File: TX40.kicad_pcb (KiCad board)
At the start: 2 copper layers, 85 x 50 mm, 16 parts, among them J1 691111710002, J2 691111710002, J3 691111710002, J4 691111710002, J5 691111710002, J6 691111710002, K1 SRD-05VDC-SL-C, K2 SRD-05VDC-SL-C

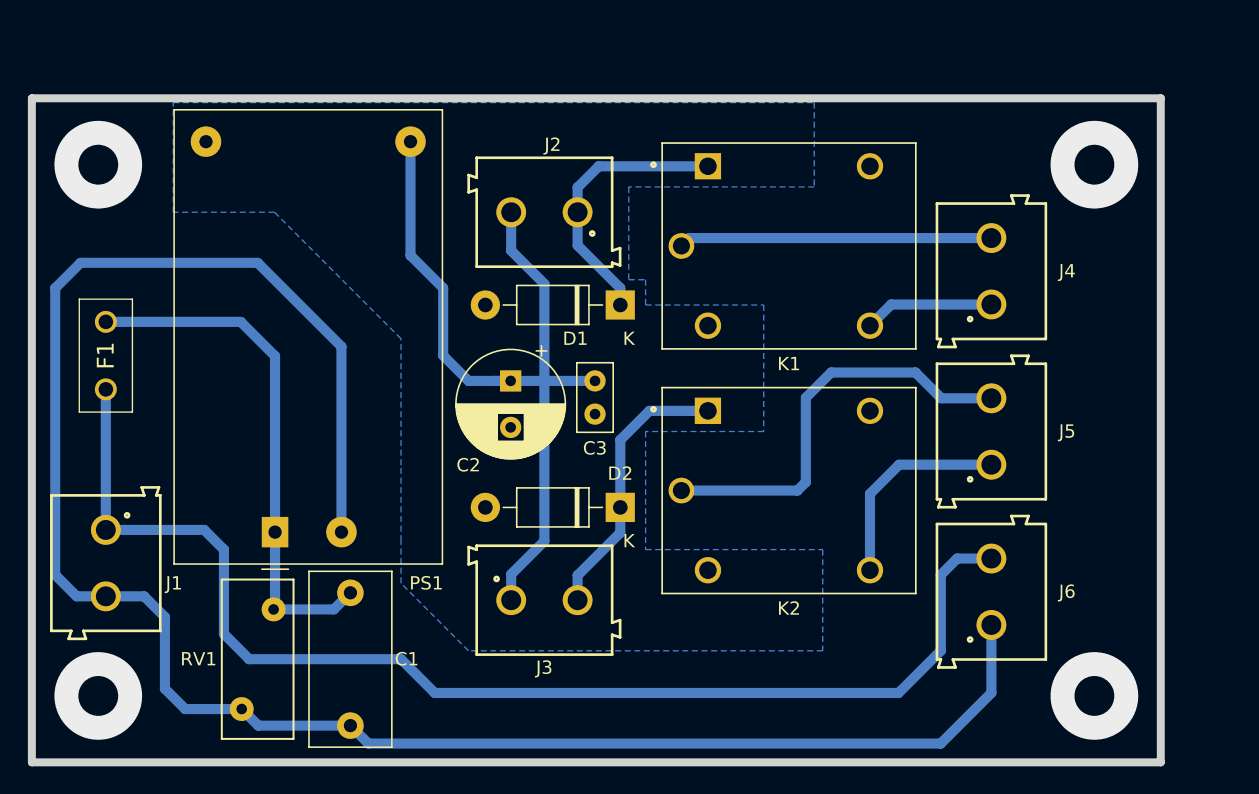
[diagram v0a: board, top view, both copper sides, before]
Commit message: Cambio a placa de 55x90
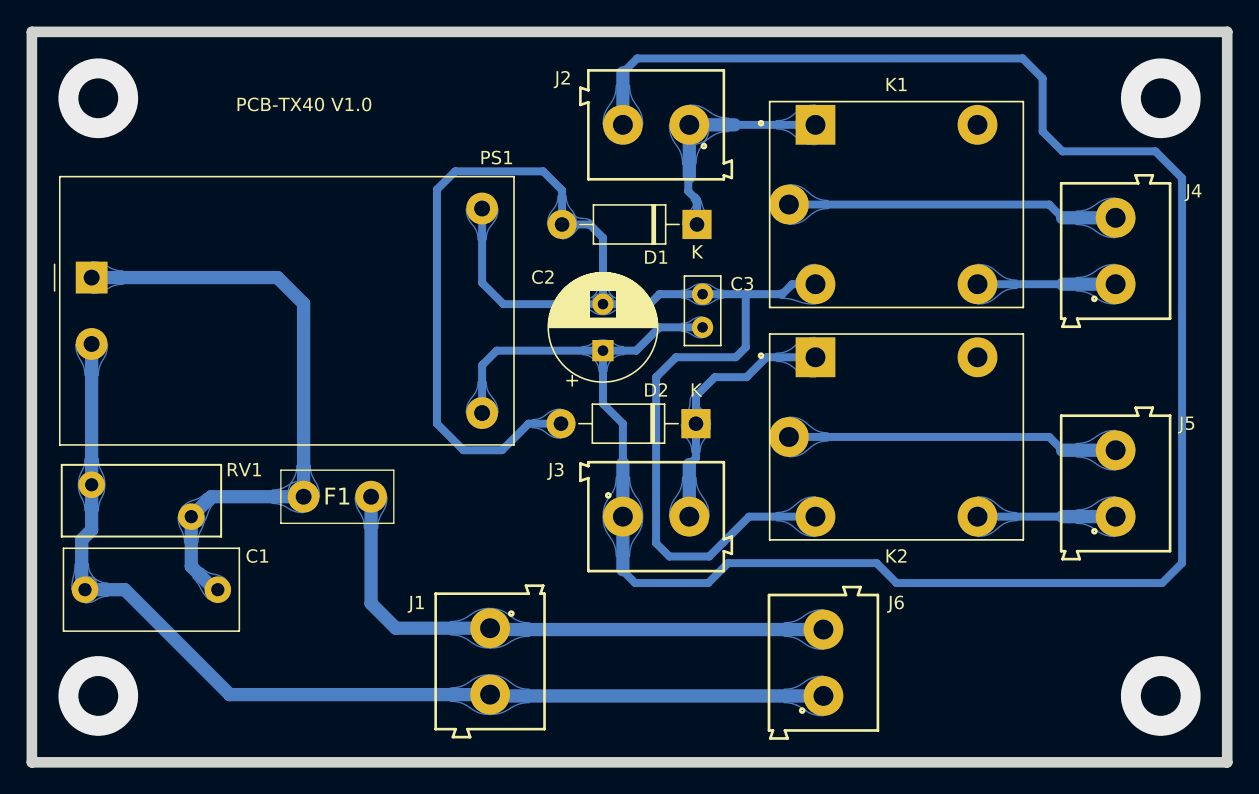
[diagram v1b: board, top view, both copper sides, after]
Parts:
- moved J1 29.9 mm to (144.5, 102.4)
- moved PS1 23.6 mm to (114.5, 73.5), turned to 0 degrees
- moved F1 21.5 mm to (135.5, 90.0), turned to 180 degrees
- moved J6 13.7 mm to (169.6, 102.5)
- moved J2 10.7 mm to (157.0, 62.0)
- moved J3 10.5 mm to (157.0, 91.5)
- moved J5 10.1 mm to (191.6, 89.0)
- moved C1 9.99 mm to (124.0, 97.0), turned to 180 degrees
- moved J4 9.48 mm to (191.6, 71.5)
- moved RV1 9.34 mm to (122.0, 91.5), turned to 180 degrees
- moved C3 9.05 mm to (160.5, 77.2), turned to 90 degrees
- moved K2 9.04 mm to (175.1, 85.5)
- moved K1 8.68 mm to (175.1, 68.0)
- moved D2 8.50 mm to (160.0, 84.5)
- moved D1 8.37 mm to (160.1, 69.5)
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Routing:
- net GND: track 0.00 -> 120.1 mm
- net +5V: track 61.9 -> 164.5 mm
- net /N: track 146.1 -> 78.0 mm
- net /L: track 93.6 -> 42.9 mm
- net /L_F1: track 39.3 -> 46.6 mm
- net /COM__K2: track 31.5 -> 25.0 mm
- net /NO__K2: track 15.8 -> 10.4 mm
- net /A1_K1: track 20.7 -> 18.9 mm
- net /COM__K1: track 23.6 -> 25.0 mm
- net /A1_K2: track 20.9 -> 19.5 mm
- net /NO__K1: track 9.80 -> 10.4 mm
- removed copper zone on B.Cu, net GND
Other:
- board size 85 x 50 mm -> 90 x 55 mm
- board text added: "PCB-TX40 V1.0"
